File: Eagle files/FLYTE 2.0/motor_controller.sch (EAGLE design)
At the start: 15 parts, among them J1 XT60PW-F

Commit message: routing done
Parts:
- added R1, R2, R3, R4: 4.7K ohm, rcl:R-US_R0805
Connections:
- new net 3V3: R1.1, R2.1, R3.1, R4.1, U1.GP21
- net SERVO1: now also R4.2
- net SERVO2: now also R1.2
- net SERVO3: now also R2.2
- net SERVO4: now also R3.2

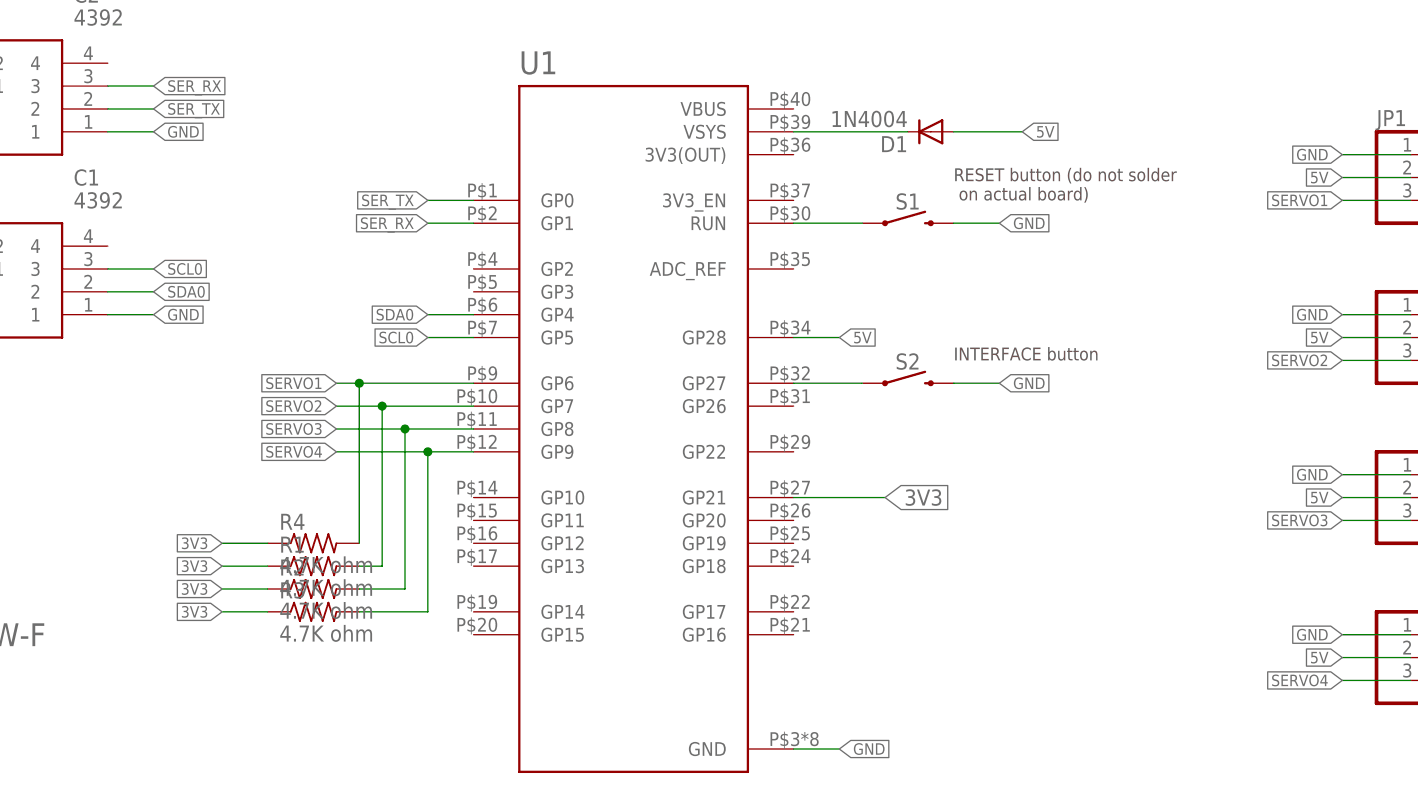
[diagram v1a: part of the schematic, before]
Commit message: Start motor conroller layout
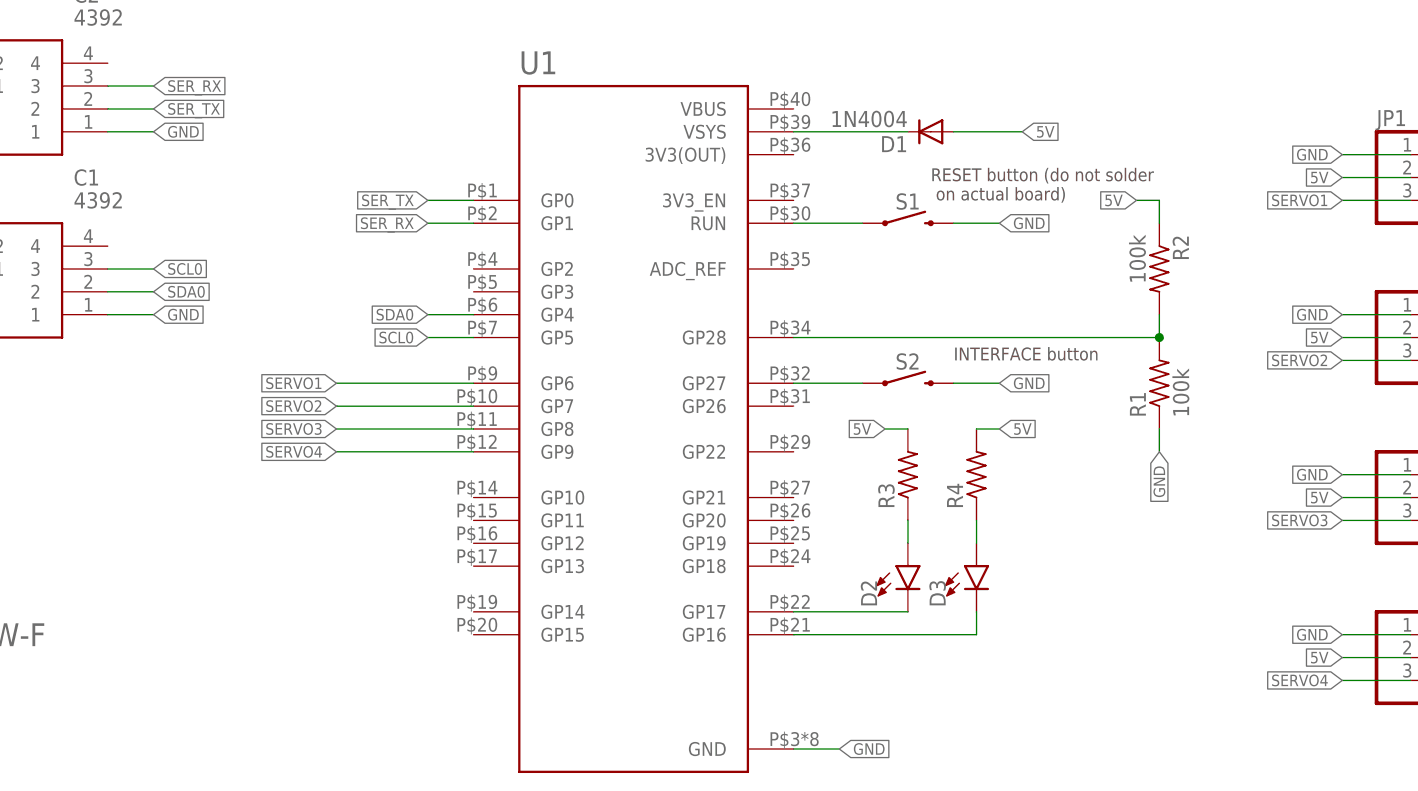
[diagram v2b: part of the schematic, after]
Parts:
- added D2, D3: (no value), SparkFun-LED:LED0603
- R1, R2: value 4.7K ohm -> 100k
- R3, R4: value 4.7K ohm -> (none)
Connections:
- removed net 3V3: R1.1, R2.1, R3.1, R4.1, U1.GP21
- new net N$4: R1.2, R2.2, U1.GP28
- new net N$5: D2.C, U1.GP17
- new net N$6: D3.C, U1.GP16
- new net N$7: D2.A, R3.1
- new net N$8: D3.A, R4.1
- net 5V: now also R2.1, R3.2, R4.2; no longer U1.GP28
- net GND: now also R1.1
- net SERVO1: no longer R4.2
- net SERVO2: no longer R1.2
- net SERVO3: no longer R2.2
- net SERVO4: no longer R3.2
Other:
- moved on the sheet: R1, R2, R3, R4

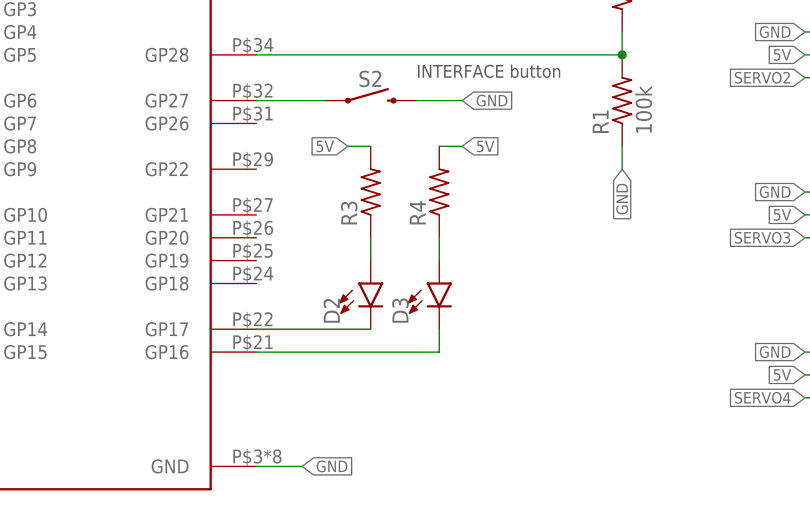
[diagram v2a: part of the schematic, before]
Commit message: Finish schematic for motor controller
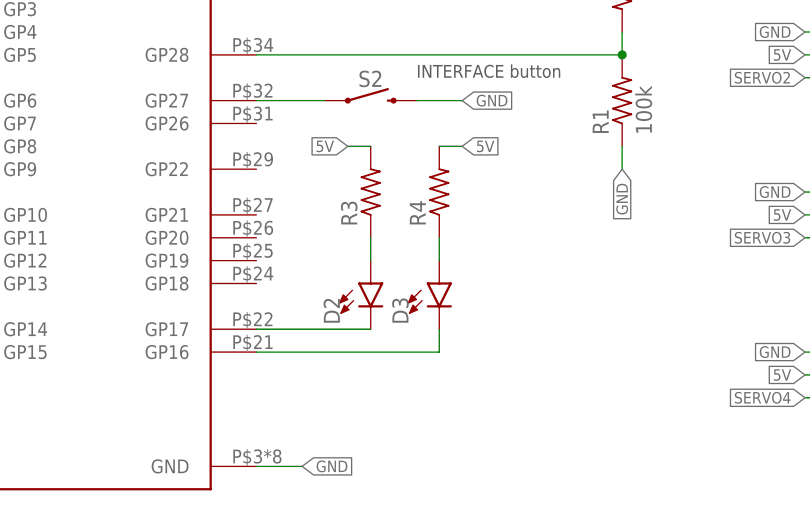
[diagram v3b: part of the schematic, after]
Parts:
- D2, D3: device SparkFun-LED:LED0603 -> led:LEDCHIPLED_1206
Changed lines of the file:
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@@
 <part name="R1" library="rcl" library_urn="urn:adsk.eagle:library:334" deviceset="R-US_" device="R0805" package3d_urn="urn:adsk.eagle:package:23553/2" value="100k"/>
 <part name="R2" library="rcl" library_urn="urn:adsk.eagle:library:334" deviceset="R-US_" device="R0805" package3d_urn="urn:adsk.eagle:package:23553/2" value="100k"/>
-<part name="D2" library="SparkFun-LED" deviceset="LED" device="0603"/>
-<part name="D3" library="SparkFun-LED" deviceset="LED" device="0603"/>
+<part name="D2" library="led" library_urn="urn:adsk.eagle:library:259" deviceset="LED" device="CHIPLED_1206" package3d_urn="urn:adsk.eagle:package:15823/2"/>
+<part name="D3" library="led" library_urn="urn:adsk.eagle:library:259" deviceset="LED" device="CHIPLED_1206" package3d_urn="urn:adsk.eagle:package:15823/2"/>
 <part name="R3" library="rcl" library_urn="urn:adsk.eagle:library:334" deviceset="R-US_" device="R0805" package3d_urn="urn:adsk.eagle:package:23553/2"/>
 <part name="R4" library="rcl" library_urn="urn:adsk.eagle:library:334" deviceset="R-US_" device="R0805" package3d_urn="urn:adsk.eagle:package:23553/2"/>
@@
 <attribute name="VALUE" x="149.098" y="82.55" size="1.778" layer="96" rot="R270"/>
 </instance>
-<instance part="D2" gate="D1" x="124.46" y="45.72" smashed="yes">
+<instance part="D2" gate="G$1" x="124.46" y="45.72" smashed="yes">
 <attribute name="NAME" x="121.031" y="41.148" size="1.778" layer="95" font="vector" rot="R90"/>
 <attribute name="VALUE" x="126.365" y="41.148" size="1.778" layer="96" font="vector" rot="R90" align="top-left"/>
 </instance>
-<instance part="D3" gate="D1" x="132.08" y="45.72" smashed="yes">
+<instance part="D3" gate="G$1" x="132.08" y="45.72" smashed="yes">
 <attribute name="NAME" x="128.651" y="41.148" size="1.778" layer="95" font="vector" rot="R90"/>
 <attribute name="VALUE" x="133.985" y="41.148" size="1.778" layer="96" font="vector" rot="R90" align="top-left"/>
@@
 <net name="N$5" class="0">
 <segment>
-<pinref part="D2" gate="D1" pin="C"/>
+<pinref part="D2" gate="G$1" pin="C"/>
 <pinref part="U1" gate="G$1" pin="GP17"/>
 <wire x1="124.46" y1="40.64" x2="111.76" y2="40.64" width="0.1524" layer="91"/>
@@
 <pinref part="U1" gate="G$1" pin="GP16"/>
 <wire x1="111.76" y1="38.1" x2="132.08" y2="38.1" width="0.1524" layer="91"/>
-<pinref part="D3" gate="D1" pin="C"/>
+<pinref part="D3" gate="G$1" pin="C"/>
 <wire x1="132.08" y1="38.1" x2="132.08" y2="40.64" width="0.1524" layer="91"/>
 </segment>
@@
 <segment>
 <pinref part="R3" gate="G$1" pin="1"/>
-<pinref part="D2" gate="D1" pin="A"/>
+<pinref part="D2" gate="G$1" pin="A"/>
 <wire x1="124.46" y1="50.8" x2="124.46" y2="48.26" width="0.1524" layer="91"/>
 </segment>
@@
 <segment>
 <pinref part="R4" gate="G$1" pin="1"/>
-<pinref part="D3" gate="D1" pin="A"/>
+<pinref part="D3" gate="G$1" pin="A"/>
 <wire x1="132.08" y1="50.8" x2="132.08" y2="48.26" width="0.1524" layer="91"/>
 </segment>

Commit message: Aur thoda
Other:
- note added: "POWER comes from an external buck converter (7.4V -> 5V)"
- moved on the sheet: C1, C2, D1, D2, D3, H1, H2, H3, H4, J1, JP1, R1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

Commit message: Finish motor controller
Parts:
- renumbered JP1 to SERVO1, JP2 to SERVO2, JP3 to SERVO3, JP4 to SERVO4, U1 to PICO
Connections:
- removed net N$7: D2.A, R3.1
- removed net N$8: D3.A, R4.1
- new net LED1: PICO.GP2, R3.1
- new net LED2: PICO.GP3, R4.1
- net 5V: now also D2.A, D3.A; no longer R3.2, R4.2
- net N$5: now also R3.2; no longer PICO.GP17
- net N$6: now also R4.2; no longer PICO.GP16
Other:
- moved on the sheet: D2, D3, R3, R4

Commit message: idk
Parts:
- removed D2, D3: (no value), led:LEDCHIPLED_1206
- removed R3, R4: (no value), rcl:R-US_R0805
- added BATTERY_REGULATOR3V1, BATTERY_REGULATOR3V3: AMS1117-3.3, AMS1117-3.3:AMS1117-3.3
- added C3, C4, C5, C6: 22uF, SparkFun-Capacitors:22UF-0805-6.3V-20%
- added LED1, LED2: WS2812B3535, WS2812B:WS2812B3535
- added R5: 4.7v, rcl:R-US_R0805
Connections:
- removed net LED1: PICO.GP2, R3.1
- removed net LED2: PICO.GP3, R4.1
- removed net N$5: D2.C, R3.2
- removed net N$6: D3.C, R4.2
- new net 3.3V: R2.1
- new net 3V3: BATTERY_REGULATOR3V3.VOUT, C3.2, D1.A
- new net 7.4V: BATTERY_REGULATOR3V1.VIN, BATTERY_REGULATOR3V3.VIN, C4.2, C5.2, J1.1, SERVO1.2, SERVO2.2, SERVO3.2, SERVO4.2
- new net LED: PICO.GP15, R5.2
- new net N$7: LED1.DO, LED2.DI
- new net N$8: LED1.DI, R5.1
- net 5V: now also BATTERY_REGULATOR3V1.VOUT, C6.2, LED1.VDD, LED2.VDD; no longer D1.A, D2.A, D3.A, J1.1, R2.1, SERVO1.2, SERVO2.2, SERVO3.2, SERVO4.2
- net GND: now also BATTERY_REGULATOR3V1.ADJ/GND, BATTERY_REGULATOR3V3.ADJ/GND, C3.1, C4.1, C5.1, C6.1, LED1.GND, LED2.GND
